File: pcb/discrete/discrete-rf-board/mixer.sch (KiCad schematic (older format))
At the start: 51 parts, among them J7 UFL, J8 UFL, Q1 NSVT65011MW6T1G, Q2 BCM857BS-7-F, Q3 Q_NPN_BCE, Q4 BCM857BS-7-F, Q5 NSVT65011MW6T1G, T1 HHM1515B2, U3 LT5560EDD#PBF

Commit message: Autofill
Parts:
- C17, C26, C31, C32, C34: footprint (none) -> Capacitor_SMD:C_0402_1005Metric; Mouser (none) -> 791-RF15N101J250CT
- C27: footprint (none) -> Capacitor_SMD:C_0402_1005Metric; Mouser (none) -> NoPart
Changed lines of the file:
@@
 F 0 "C26" H 5408 2996 50  0000 R CNN
 F 1 "100 pF RF" H 5408 2905 50  0000 R CNN
-F 2 "" H 5500 2950 50  0001 C CNN
+F 2 "Capacitor_SMD:C_0402_1005Metric" H 5500 2950 50  0001 C CNN
 F 3 "~" H 5500 2950 50  0001 C CNN
+F 4 "791-RF15N101J250CT " H 5500 2950 50  0001 C CNN "Mouser"
 	1    5500 2950
 	0    -1   -1   0
@@
 F 0 "C34" H 9110 3120 50  0000 L CNN
 F 1 "100 pF" H 9110 2970 50  0000 L CNN
-F 2 "" H 9100 3050 50  0001 C CNN
+F 2 "Capacitor_SMD:C_0402_1005Metric" H 9100 3050 50  0001 C CNN
 F 3 "~" H 9100 3050 50  0001 C CNN
+F 4 "791-RF15N101J250CT " H 9100 3050 50  0001 C CNN "Mouser"
 	1    9100 3050
 	1    0    0    -1
@@
 F 0 "C32" H 8710 3120 50  0000 L CNN
 F 1 "100 pF" H 8710 2970 50  0000 L CNN
-F 2 "" H 8700 3050 50  0001 C CNN
+F 2 "Capacitor_SMD:C_0402_1005Metric" H 8700 3050 50  0001 C CNN
 F 3 "~" H 8700 3050 50  0001 C CNN
+F 4 "791-RF15N101J250CT " H 8700 3050 50  0001 C CNN "Mouser"
 	1    8700 3050
 	1    0    0    -1
@@
 F 0 "C31" H 8360 3120 50  0000 L CNN
 F 1 "100 pF" H 8360 2970 50  0000 L CNN
-F 2 "" H 8350 3050 50  0001 C CNN
+F 2 "Capacitor_SMD:C_0402_1005Metric" H 8350 3050 50  0001 C CNN
 F 3 "~" H 8350 3050 50  0001 C CNN
+F 4 "791-RF15N101J250CT " H 8350 3050 50  0001 C CNN "Mouser"
 	1    8350 3050
 	1    0    0    -1
@@
 F 0 "C17" H 3510 6470 50  0000 L CNN
 F 1 "100 pF" H 3510 6320 50  0000 L CNN
-F 2 "" H 3500 6400 50  0001 C CNN
+F 2 "Capacitor_SMD:C_0402_1005Metric" H 3500 6400 50  0001 C CNN
 F 3 "~" H 3500 6400 50  0001 C CNN
+F 4 "791-RF15N101J250CT " H 3500 6400 50  0001 C CNN "Mouser"
 	1    3500 6400
 	1    0    0    -1
@@
 F 0 "C27" H 5760 3270 50  0000 L CNN
 F 1 "DNP 0402" H 5760 3120 50  0000 L CNN
-F 2 "" H 5750 3200 50  0001 C CNN
+F 2 "Capacitor_SMD:C_0402_1005Metric" H 5750 3200 50  0001 C CNN
 F 3 "~" H 5750 3200 50  0001 C CNN
+F 4 "NoPart" H 5750 3200 50  0001 C CNN "Mouser"
 	1    5750 3200
 	1    0    0    -1

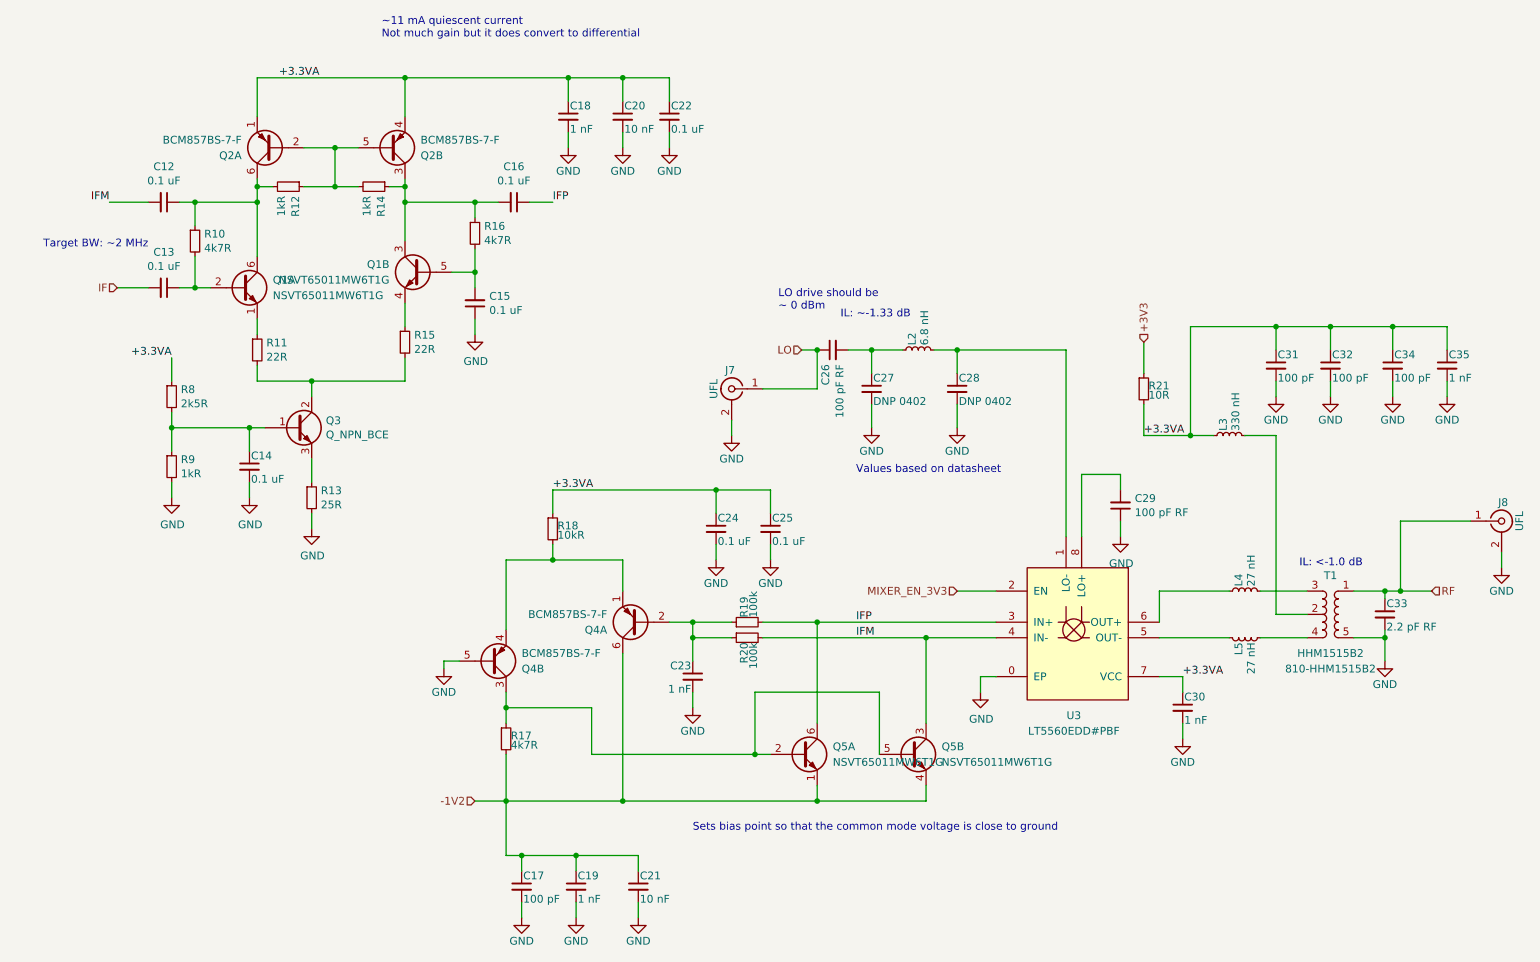
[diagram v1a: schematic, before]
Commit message: Add more footprints, saving before autofill
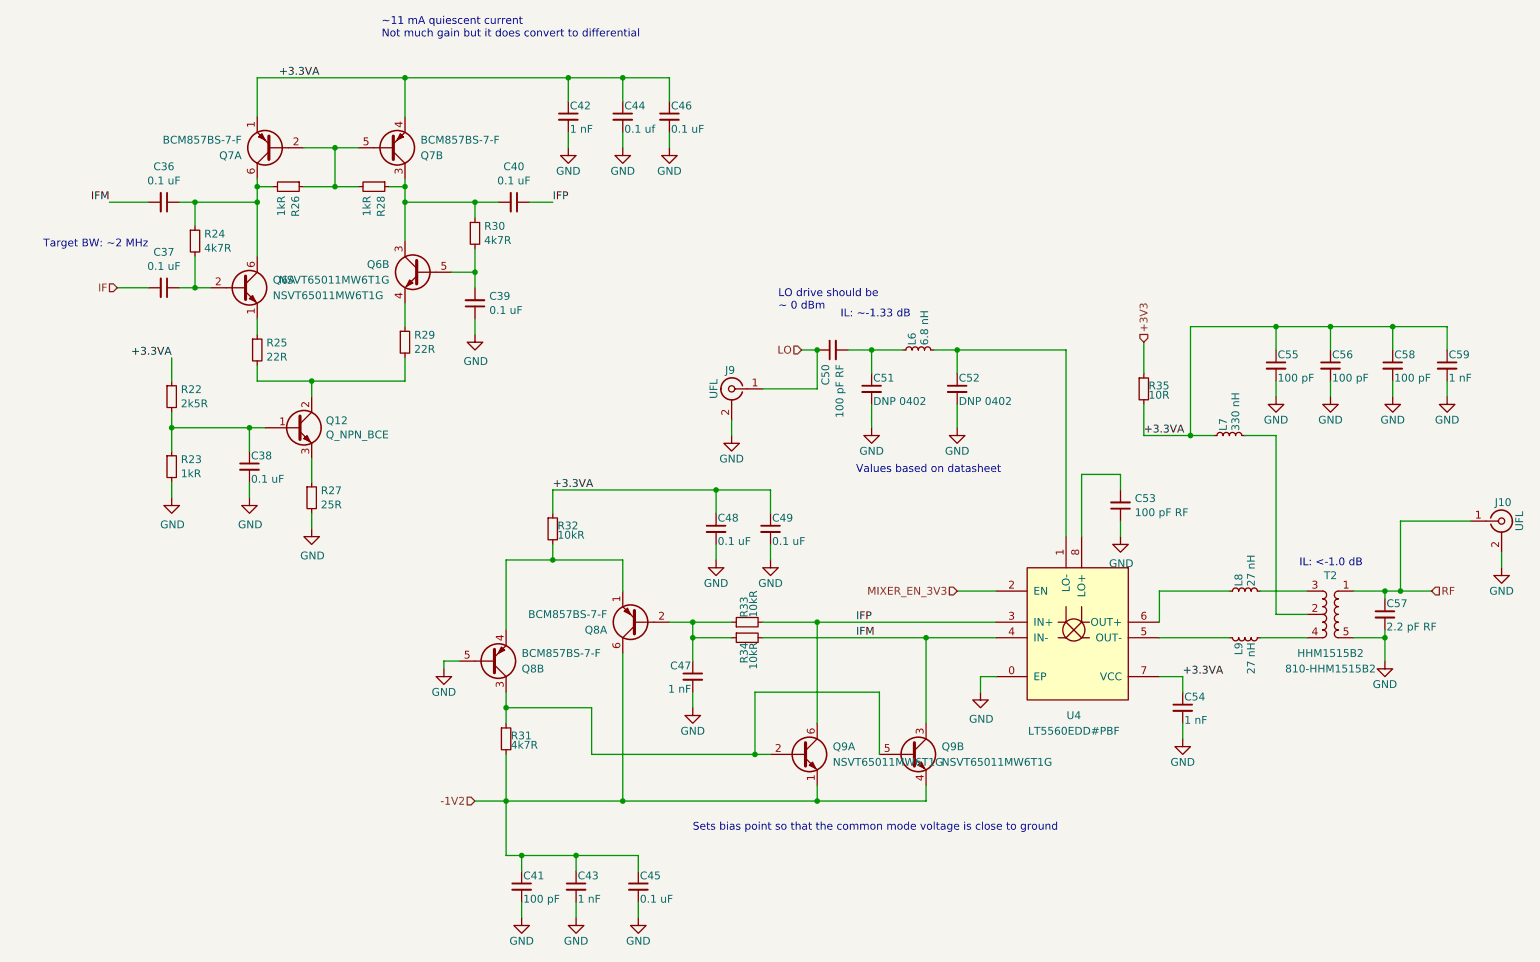
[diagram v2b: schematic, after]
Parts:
- C14: footprint (none) -> Capacitor_SMD:C_0402_1005Metric; Mouser (none) -> 80-C0402C104M4P
- C20: value 10 nF -> 0.1 uf
- C21: value 10 nF -> 0.1 uF
- R19, R20: value 100k -> 10kR

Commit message: Autofill
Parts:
- C12, C13, C15, C16, C21, C22, C24, C25: footprint (none) -> Capacitor_SMD:C_0402_1005Metric; Mouser (none) -> 80-C0402C104M4P
- R18, R19, R20: footprint (none) -> Resistor_SMD:R_0402_1005Metric; Mouser (none) -> 603-AC0402FR-1310KL
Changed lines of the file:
@@
 F 0 "R33" H 4980 4720 50  0000 L CNN
 F 1 "10kR" H 4980 4660 50  0000 L CNN
-F 2 "" H 4950 4700 50  0001 C CNN
+F 2 "Resistor_SMD:R_0402_1005Metric" H 4950 4700 50  0001 C CNN
 F 3 "~" H 4950 4700 50  0001 C CNN
+F 4 "603-AC0402FR-1310KL" H 4950 4700 50  0001 C CNN "Mouser"
 	1    4950 4700
 	0    -1   -1   0
@@
 F 0 "R34" H 4980 4820 50  0000 L CNN
 F 1 "10kR" H 4980 4760 50  0000 L CNN
-F 2 "" H 4950 4800 50  0001 C CNN
+F 2 "Resistor_SMD:R_0402_1005Metric" H 4950 4800 50  0001 C CNN
 F 3 "~" H 4950 4800 50  0001 C CNN
+F 4 "603-AC0402FR-1310KL" H 4950 4800 50  0001 C CNN "Mouser"
 	1    4950 4800
 	0    -1   1    0
@@
 F 0 "R32" H 3730 4120 50  0000 L CNN
 F 1 "10kR" H 3730 4060 50  0000 L CNN
-F 2 "" H 3700 4100 50  0001 C CNN
+F 2 "Resistor_SMD:R_0402_1005Metric" H 3700 4100 50  0001 C CNN
 F 3 "~" H 3700 4100 50  0001 C CNN
+F 4 "603-AC0402FR-1310KL" H 3700 4100 50  0001 C CNN "Mouser"
 	1    3700 4100
 	1    0    0    -1
@@
 F 0 "C45" H 4260 6470 50  0000 L CNN
 F 1 "0.1 uF" H 4260 6320 50  0000 L CNN
-F 2 "" H 4250 6400 50  0001 C CNN
+F 2 "Capacitor_SMD:C_0402_1005Metric" H 4250 6400 50  0001 C CNN
 F 3 "~" H 4250 6400 50  0001 C CNN
+F 4 "80-C0402C104M4P" H 4250 6400 50  0001 C CNN "Mouser"
 	1    4250 6400
 	1    0    0    -1
@@
 F 0 "C37" V 971 2550 50  0000 C CNN
 F 1 "0.1 uF" V 1062 2550 50  0000 C CNN
-F 2 "" H 1200 2550 50  0001 C CNN
+F 2 "Capacitor_SMD:C_0402_1005Metric" H 1200 2550 50  0001 C CNN
 F 3 "~" H 1200 2550 50  0001 C CNN
+F 4 "80-C0402C104M4P" H 1200 2550 50  0001 C CNN "Mouser"
 	1    1200 2550
 	0    1    1    0
@@
 F 0 "C39" H 3108 2604 50  0000 R CNN
 F 1 "0.1 uF" H 3108 2695 50  0000 R CNN
-F 2 "" H 3200 2650 50  0001 C CNN
+F 2 "Capacitor_SMD:C_0402_1005Metric" H 3200 2650 50  0001 C CNN
 F 3 "~" H 3200 2650 50  0001 C CNN
+F 4 "80-C0402C104M4P" H 3200 2650 50  0001 C CNN "Mouser"
 	1    3200 2650
 	-1   0    0    1
@@
 F 0 "C36" V 971 2000 50  0000 C CNN
 F 1 "0.1 uF" V 1062 2000 50  0000 C CNN
-F 2 "" H 1200 2000 50  0001 C CNN
+F 2 "Capacitor_SMD:C_0402_1005Metric" H 1200 2000 50  0001 C CNN
 F 3 "~" H 1200 2000 50  0001 C CNN
+F 4 "80-C0402C104M4P" H 1200 2000 50  0001 C CNN "Mouser"
 	1    1200 2000
 	0    1    1    0
@@
 F 0 "C40" V 3221 2000 50  0000 C CNN
 F 1 "0.1 uF" V 3312 2000 50  0000 C CNN
-F 2 "" H 3450 2000 50  0001 C CNN
+F 2 "Capacitor_SMD:C_0402_1005Metric" H 3450 2000 50  0001 C CNN
 F 3 "~" H 3450 2000 50  0001 C CNN
+F 4 "80-C0402C104M4P" H 3450 2000 50  0001 C CNN "Mouser"
 	1    3450 2000
 	0    1    1    0
@@
 F 0 "C48" H 4760 4170 50  0000 L CNN
 F 1 "0.1 uF" H 4760 4020 50  0000 L CNN
-F 2 "" H 4750 4100 50  0001 C CNN
+F 2 "Capacitor_SMD:C_0402_1005Metric" H 4750 4100 50  0001 C CNN
 F 3 "~" H 4750 4100 50  0001 C CNN
+F 4 "80-C0402C104M4P" H 4750 4100 50  0001 C CNN "Mouser"
 	1    4750 4100
 	1    0    0    -1
@@
 F 0 "C49" H 5110 4170 50  0000 L CNN
 F 1 "0.1 uF" H 5110 4020 50  0000 L CNN
-F 2 "" H 5100 4100 50  0001 C CNN
+F 2 "Capacitor_SMD:C_0402_1005Metric" H 5100 4100 50  0001 C CNN
 F 3 "~" H 5100 4100 50  0001 C CNN
+F 4 "80-C0402C104M4P" H 5100 4100 50  0001 C CNN "Mouser"
 	1    5100 4100
 	1    0    0    -1
@@
 F 0 "C46" H 4460 1520 50  0000 L CNN
 F 1 "0.1 uF" H 4460 1370 50  0000 L CNN
-F 2 "" H 4450 1450 50  0001 C CNN
+F 2 "Capacitor_SMD:C_0402_1005Metric" H 4450 1450 50  0001 C CNN
 F 3 "~" H 4450 1450 50  0001 C CNN
+F 4 "80-C0402C104M4P" H 4450 1450 50  0001 C CNN "Mouser"
 	1    4450 1450
 	1    0    0    -1

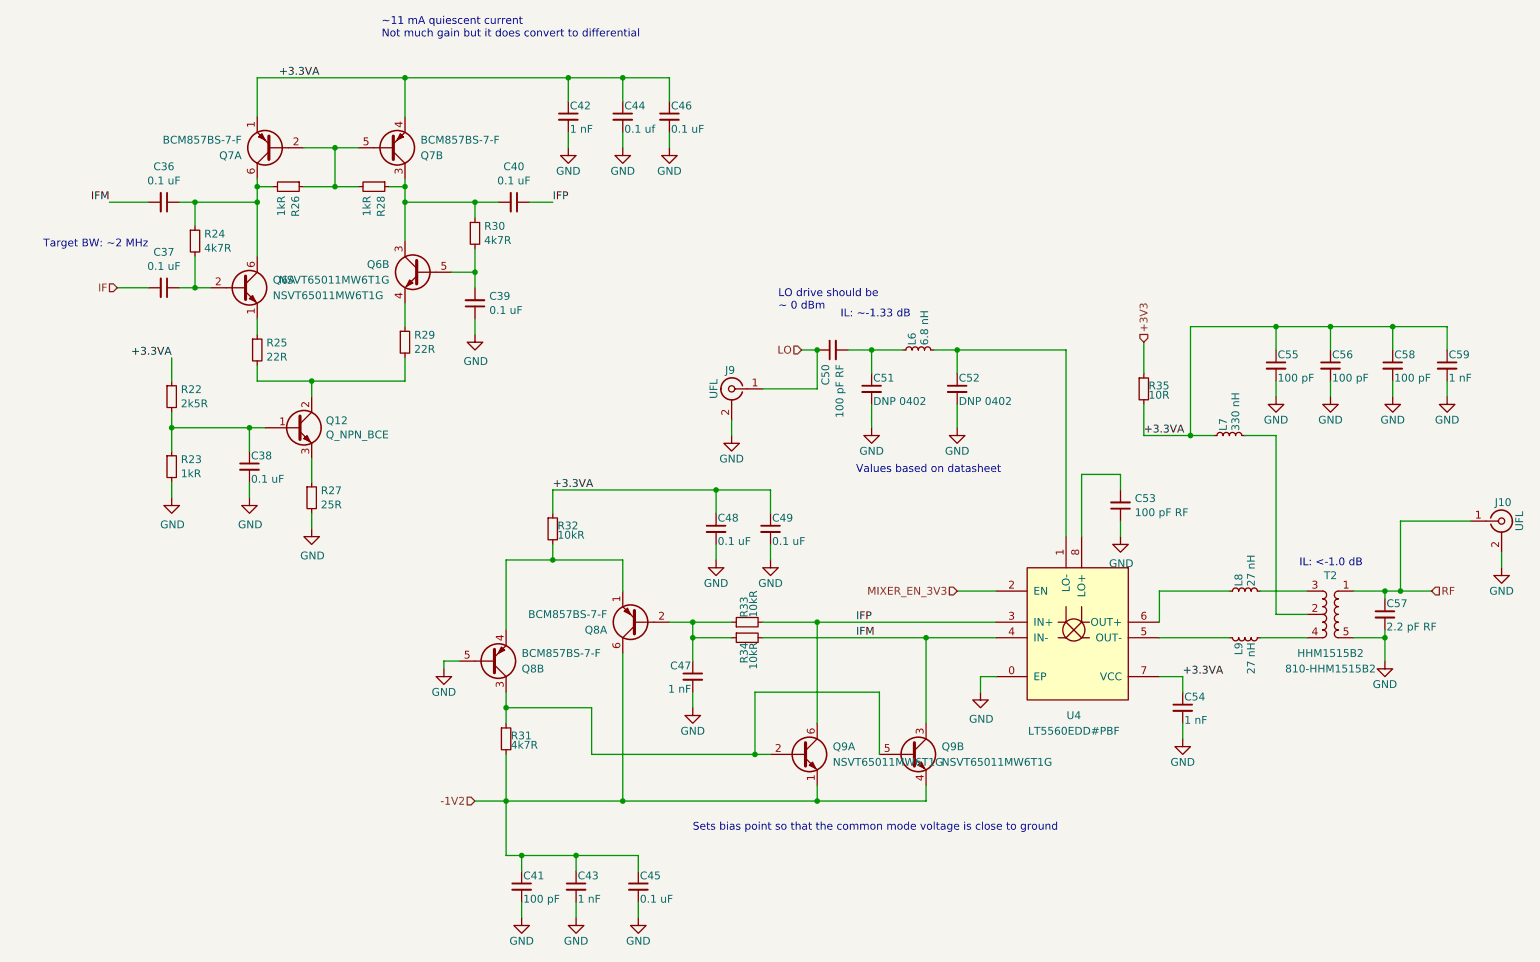
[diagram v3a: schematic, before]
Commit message: Reannotate everything; I'm trying to cut down the number of components
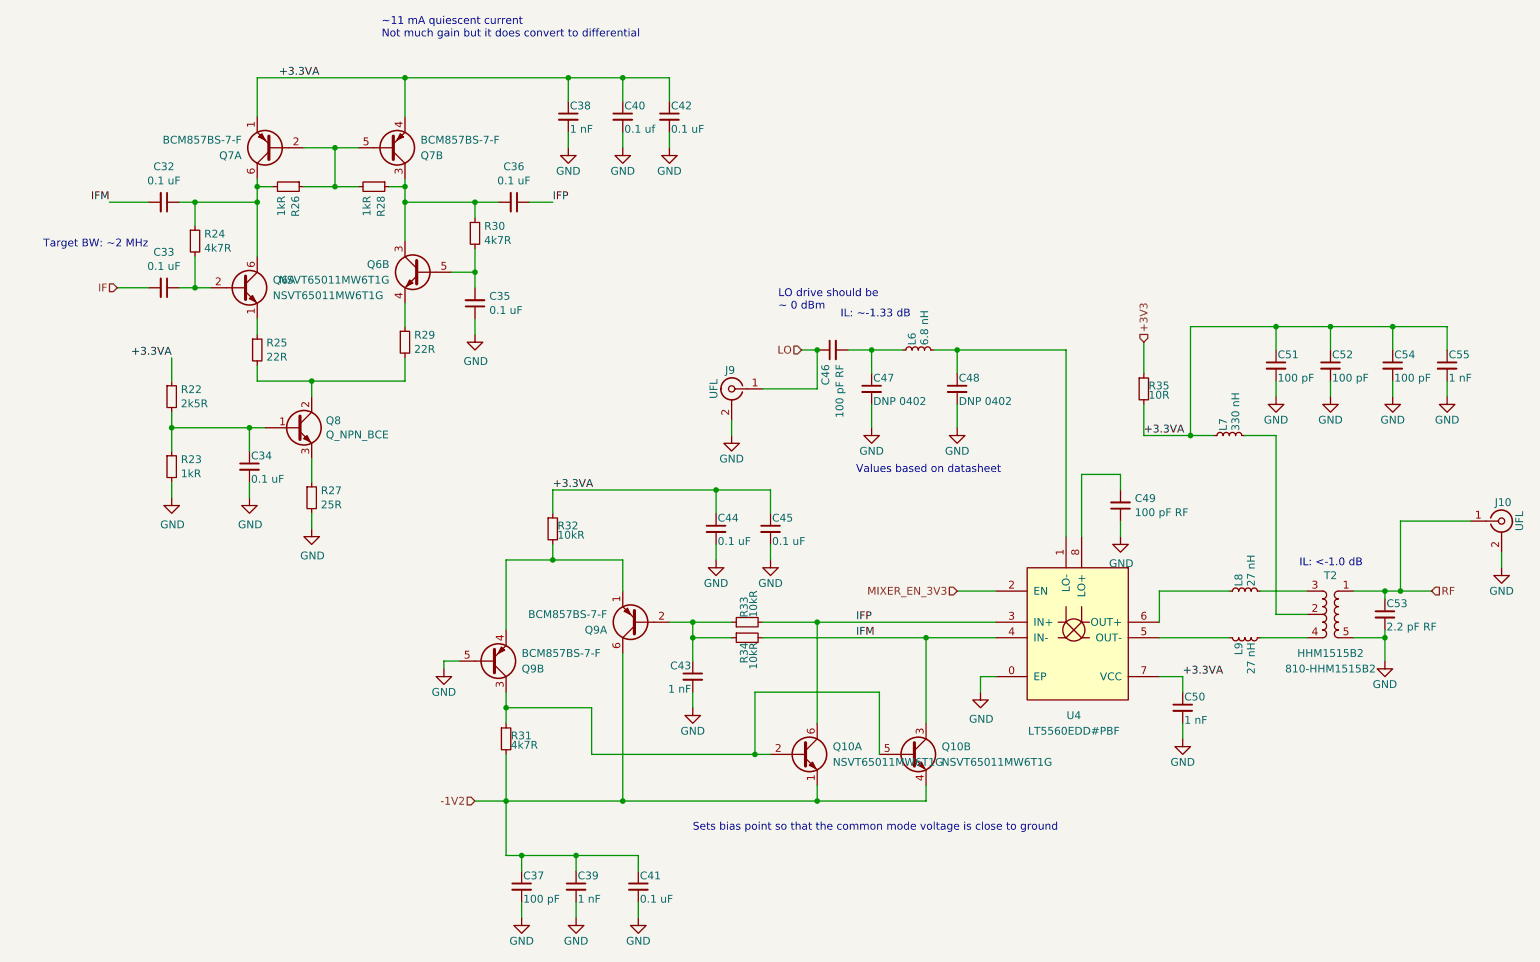
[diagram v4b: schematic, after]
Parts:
- renumbered C14 to C10, C15 to C11, C16 to C12, C17 to C13, C18 to C14, C19 to C15, C20 to C16, C21 to C17, C22 to C18, C23 to C19, C24 to C20, C25 to C21, C26 to C22, C27 to C23, C28 to C24, C29 to C25, C30 to C26, C31 to C27, C32 to C28, C33 to C29, C34 to C30, C35 to C31, C12 to C8, C13 to C9

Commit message: Footprint a lot of stuff; save before autofill
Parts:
- removed L3: 330 nH, symbol Device:L_Small
- C16: value 0.1 uf -> 0.1 uF
- C29: footprint (none) -> Capacitor_SMD:C_0402_1005Metric; Mouser (none) -> 791-RF15N2R2C500CT
- L4: footprint (none) -> Capacitor_SMD:C_0402_1005Metric; Mouser (none) -> 81-LQG15HN27NH02D
- R13: value 25R -> 22R
- R21: value 10R -> 22R; footprint (none) -> Resistor_SMD:R_0402_1005Metric; Mouser (none) -> 71-CRCW040222R0JNEDC
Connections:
- net +3.3VA: now also T1.2 (COMMON)
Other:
- note added: "TODO adjust biasing resistors to use more common values;\n2.5kR isn't common"

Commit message: Autofill
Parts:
- C14, C15, C19, C26, C31: footprint (none) -> Capacitor_SMD:C_0402_1005Metric; Mouser (none) -> 80-C0402C102K5R7411
- C16: footprint (none) -> Capacitor_SMD:C_0402_1005Metric; Mouser (none) -> 80-C0402C104M4P
- L5: footprint (none) -> Capacitor_SMD:C_0402_1005Metric; Mouser (none) -> 81-LQG15HN27NH02D
- R11, R13, R15: footprint (none) -> Resistor_SMD:R_0402_1005Metric; Mouser (none) -> 71-CRCW040222R0JNEDC
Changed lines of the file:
@@
 F 0 "C26" H 7760 5320 50  0000 L CNN
 F 1 "1 nF" H 7760 5170 50  0000 L CNN
-F 2 "" H 7750 5250 50  0001 C CNN
+F 2 "Capacitor_SMD:C_0402_1005Metric" H 7750 5250 50  0001 C CNN
 F 3 "~" H 7750 5250 50  0001 C CNN
+F 4 "80-C0402C102K5R7411" H 7750 5250 50  0001 C CNN "Mouser"
 	1    7750 5250
 	1    0    0    -1
@@
 F 0 "C31" H 9460 3120 50  0000 L CNN
 F 1 "1 nF" H 9460 2970 50  0000 L CNN
-F 2 "" H 9450 3050 50  0001 C CNN
+F 2 "Capacitor_SMD:C_0402_1005Metric" H 9450 3050 50  0001 C CNN
 F 3 "~" H 9450 3050 50  0001 C CNN
+F 4 "80-C0402C102K5R7411" H 9450 3050 50  0001 C CNN "Mouser"
 	1    9450 3050
 	1    0    0    -1
@@
 F 0 "L5" H 8180 4840 50  0000 L CNN
 F 1 "27 nH" H 8180 4760 50  0000 L CNN
-F 2 "" H 8150 4800 50  0001 C CNN
+F 2 "Capacitor_SMD:C_0402_1005Metric" H 8150 4800 50  0001 C CNN
 F 3 "~" H 8150 4800 50  0001 C CNN
+F 4 "81-LQG15HN27NH02D" H 8150 4800 50  0001 C CNN "Mouser"
 	1    8150 4800
 	0    -1   1    0
@@
 F 0 "C19" H 4610 5120 50  0000 L CNN
 F 1 "1 nF" H 4610 4970 50  0000 L CNN
-F 2 "" H 4600 5050 50  0001 C CNN
+F 2 "Capacitor_SMD:C_0402_1005Metric" H 4600 5050 50  0001 C CNN
 F 3 "~" H 4600 5050 50  0001 C CNN
+F 4 "80-C0402C102K5R7411" H 4600 5050 50  0001 C CNN "Mouser"
 	1    4600 5050
 	-1   0    0    -1
@@
 F 0 "C15" H 3860 6470 50  0000 L CNN
 F 1 "1 nF" H 3860 6320 50  0000 L CNN
-F 2 "" H 3850 6400 50  0001 C CNN
+F 2 "Capacitor_SMD:C_0402_1005Metric" H 3850 6400 50  0001 C CNN
 F 3 "~" H 3850 6400 50  0001 C CNN
+F 4 "80-C0402C102K5R7411" H 3850 6400 50  0001 C CNN "Mouser"
 	1    3850 6400
 	1    0    0    -1
@@
 F 0 "R11" H 1859 2996 50  0000 L CNN
 F 1 "22R" H 1859 2905 50  0000 L CNN
-F 2 "" H 1800 2950 50  0001 C CNN
+F 2 "Resistor_SMD:R_0402_1005Metric" H 1800 2950 50  0001 C CNN
 F 3 "~" H 1800 2950 50  0001 C CNN
+F 4 "71-CRCW040222R0JNEDC" H 1800 2950 50  0001 C CNN "Mouser"
 	1    1800 2950
 	1    0    0    -1
@@
 F 0 "R15" H 2809 2946 50  0000 L CNN
 F 1 "22R" H 2809 2855 50  0000 L CNN
-F 2 "" H 2750 2900 50  0001 C CNN
+F 2 "Resistor_SMD:R_0402_1005Metric" H 2750 2900 50  0001 C CNN
 F 3 "~" H 2750 2900 50  0001 C CNN
+F 4 "71-CRCW040222R0JNEDC" H 2750 2900 50  0001 C CNN "Mouser"
 	1    2750 2900
 	1    0    0    -1
@@
 F 0 "R13" H 2209 3946 50  0000 L CNN
 F 1 "22R" H 2209 3855 50  0000 L CNN
-F 2 "" H 2150 3900 50  0001 C CNN
+F 2 "Resistor_SMD:R_0402_1005Metric" H 2150 3900 50  0001 C CNN
 F 3 "~" H 2150 3900 50  0001 C CNN
+F 4 "71-CRCW040222R0JNEDC" H 2150 3900 50  0001 C CNN "Mouser"
 	1    2150 3900
 	1    0    0    -1
@@
 F 0 "C14" H 3810 1520 50  0000 L CNN
 F 1 "1 nF" H 3810 1370 50  0000 L CNN
-F 2 "" H 3800 1450 50  0001 C CNN
+F 2 "Capacitor_SMD:C_0402_1005Metric" H 3800 1450 50  0001 C CNN
 F 3 "~" H 3800 1450 50  0001 C CNN
+F 4 "80-C0402C102K5R7411" H 3800 1450 50  0001 C CNN "Mouser"
 	1    3800 1450
 	1    0    0    -1
@@
 F 0 "C16" H 4160 1520 50  0000 L CNN
 F 1 "0.1 uF" H 4160 1370 50  0000 L CNN
-F 2 "" H 4150 1450 50  0001 C CNN
+F 2 "Capacitor_SMD:C_0402_1005Metric" H 4150 1450 50  0001 C CNN
 F 3 "~" H 4150 1450 50  0001 C CNN
+F 4 "80-C0402C104M4P" H 4150 1450 50  0001 C CNN "Mouser"
 	1    4150 1450
 	1    0    0    -1

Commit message: Add in a couple more components, save before autofill
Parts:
- R8: value 2k5R -> 2k7R; footprint (none) -> Resistor_SMD:R_0402_1005Metric; Mouser (none) -> 652-CR0402JW-272GLF
